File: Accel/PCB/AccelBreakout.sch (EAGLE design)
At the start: 9 parts, among them U1 MMA8653FCR1

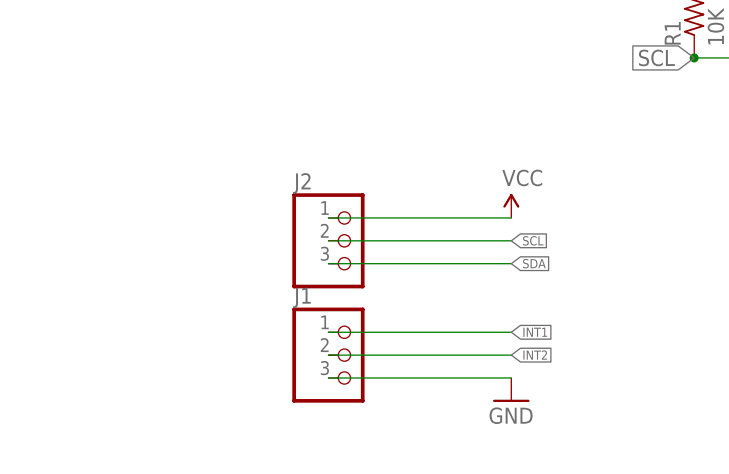
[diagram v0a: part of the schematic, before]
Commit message: added reverse voltage protection
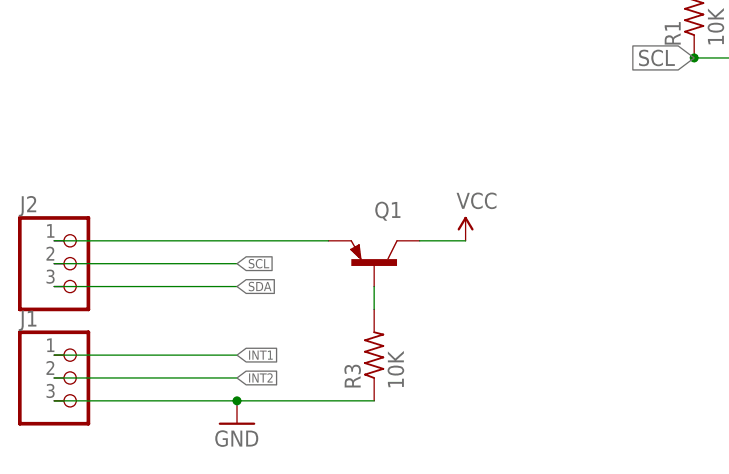
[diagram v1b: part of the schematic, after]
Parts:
- added Q1: MMBTA56-SOT23, transistor-pnp:MMBTA56-SOT23
- added R3: 10K, AccelBreakout:R-US_R0603
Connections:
- new net N$1: J2.1, Q1.E
- new net N$2: Q1.B, R3.2
- net GND: now also R3.1
- net VCC: now also Q1.C; no longer J2.1
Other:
- moved on the sheet: J1, J2
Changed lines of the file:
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@@
 <?xml version="1.0" encoding="utf-8"?>
 <!DOCTYPE eagle SYSTEM "eagle.dtd">
-<eagle version="7.1.0">
+<eagle version="7.6.0">
 <drawing>
 <settings>
@@
 <setting verticaltext="up"/>
 </settings>
-<grid distance="0.1" unitdist="inch" unit="inch" style="lines" multiple="1" display="yes" altdistance="0.01" altunitdist="inch" altunit="inch"/>
+<grid distance="0.1" unitdist="inch" unit="inch" style="lines" multiple="1" display="no" altdistance="0.01" altunitdist="inch" altunit="inch"/>
 <layers>
 <layer number="1" name="Top" color="4" fill="1" visible="no" active="no"/>
 <layer number="2" name="Route2" color="1" fill="3" visible="no" active="no"/>
 <layer number="3" name="Route3" color="4" fill="3" visible="no" active="no"/>
+<layer number="4" name="Route4" color="1" fill="4" visible="no" active="no"/>
+<layer number="5" name="Route5" color="4" fill="4" visible="no" active="no"/>
+<layer number="6" name="Route6" color="1" fill="8" visible="no" active="no"/>
+<layer number="7" name="Route7" color="4" fill="8" visible="no" active="no"/>
+<layer number="8" name="Route8" color="1" fill="2" visible="no" active="no"/>
+<layer number="9" name="Route9" color="4" fill="2" visible="no" active="no"/>
+<layer number="10" name="Route10" color="1" fill="7" visible="no" active="no"/>
+<layer number="11" name="Route11" color="4" fill="7" visible="no" active="no"/>
+<layer number="12" name="Route12" color="1" fill="5" visible="no" active="no"/>
+<layer number="13" name="Route13" color="4" fill="5" visible="no" active="no"/>
 <layer number="14" name="Route14" color="1" fill="6" visible="no" active="no"/>
 <layer number="15" name="Route15" color="4" fill="6" visible="no" active="no"/>
@@
 <part name="J1" library="AccelBreakout" deviceset="PINHD-1X3" device=""/>
 <part name="FRAME1" library="frames" deviceset="LETTER_L" device=""/>
+<part name="Q1" library="transistor-pnp" deviceset="*-?" device="SOT23" technology="MMBTA56"/>
+<part name="R3" library="AccelBreakout" deviceset="R-US_" device="R0603" value="10K"/>
 </parts>
 <sheets>
@@
 <instance part="R1" gate="G$1" x="20.32" y="60.96" rot="R90"/>
 <instance part="R2" gate="G$1" x="83.82" y="66.04" rot="R90"/>
-<instance part="SUPPLY1" gate="G$1" x="0" y="38.1"/>
-<instance part="GND1" gate="1" x="0" y="17.78"/>
-<instance part="J2" gate="A" x="-17.78" y="35.56"/>
-<instance part="J1" gate="A" x="-17.78" y="22.86"/>
+<instance part="SUPPLY1" gate="G$1" x="-5.08" y="35.56"/>
+<instance part="GND1" gate="1" x="-30.48" y="15.24"/>
+<instance part="J2" gate="A" x="-48.26" y="33.02"/>
+<instance part="J1" gate="A" x="-48.26" y="20.32"/>
 <instance part="FRAME1" gate="G$1" x="-86.36" y="-53.34"/>
 <instance part="FRAME1" gate="G$2" x="60.96" y="-53.34"/>
+<instance part="Q1" gate="D" x="-15.24" y="33.02" smashed="yes" rot="R90">
+<attribute name="NAME" x="-15.24" y="38.1" size="1.778" layer="95"/>
+</instance>
+<instance part="R3" gate="G$1" x="-15.24" y="22.86" rot="R90"/>
 </instances>
 <busses>
@@
 </segment>
 <segment>
+<pinref part="Q1" gate="D" pin="C"/>
 <pinref part="SUPPLY1" gate="G$1" pin="VCC"/>
-<wire x1="-20.32" y1="38.1" x2="0" y2="38.1" width="0.1524" layer="91"/>
-<pinref part="J2" gate="A" pin="1"/>
+<wire x1="-10.16" y1="35.56" x2="-5.08" y2="35.56" width="0.1524" layer="91"/>
 </segment>
 </net>
@@
 <segment>
 <pinref part="GND1" gate="1" pin="GND"/>
-<wire x1="0" y1="20.32" x2="-20.32" y2="20.32" width="0.1524" layer="91"/>
+<wire x1="-30.48" y1="17.78" x2="-50.8" y2="17.78" width="0.1524" layer="91"/>
 <pinref part="J1" gate="A" pin="3"/>
+<pinref part="R3" gate="G$1" pin="1"/>
+<wire x1="-30.48" y1="17.78" x2="-15.24" y2="17.78" width="0.1524" layer="91"/>
+<junction x="-30.48" y="17.78"/>
 </segment>
 </net>
@@
 <segment>
 <pinref part="J2" gate="A" pin="3"/>
-<wire x1="-20.32" y1="33.02" x2="0" y2="33.02" width="0.1524" layer="91"/>
-<label x="0" y="33.02" size="1.016" layer="95" xref="yes"/>
+<wire x1="-50.8" y1="30.48" x2="-30.48" y2="30.48" width="0.1524" layer="91"/>
+<label x="-30.48" y="30.48" size="1.016" layer="95" xref="yes"/>
 </segment>
 </net>
@@
 <segment>
 <pinref part="J2" gate="A" pin="2"/>
-<wire x1="-20.32" y1="35.56" x2="0" y2="35.56" width="0.1524" layer="91"/>
-<label x="0" y="35.56" size="1.016" layer="95" xref="yes"/>
+<wire x1="-50.8" y1="33.02" x2="-30.48" y2="33.02" width="0.1524" layer="91"/>
+<label x="-30.48" y="33.02" size="1.016" layer="95" xref="yes"/>
 </segment>
 </net>
@@
 </segment>
 <segment>
-<label x="0" y="25.4" size="1.016" layer="95" xref="yes"/>
-<wire x1="-20.32" y1="25.4" x2="0" y2="25.4" width="0.1524" layer="91"/>
+<label x="-30.48" y="22.86" size="1.016" layer="95" xref="yes"/>
+<wire x1="-50.8" y1="22.86" x2="-30.48" y2="22.86" width="0.1524" layer="91"/>
 <pinref part="J1" gate="A" pin="1"/>
 </segment>
@@
 </segment>
 <segment>
-<label x="0" y="22.86" size="1.016" layer="95" xref="yes"/>
-<wire x1="-20.32" y1="22.86" x2="0" y2="22.86" width="0.1524" layer="91"/>
+<label x="-30.48" y="20.32" size="1.016" layer="95" xref="yes"/>
+<wire x1="-50.8" y1="20.32" x2="-30.48" y2="20.32" width="0.1524" layer="91"/>
 <pinref part="J1" gate="A" pin="2"/>
 </segment>
 </net>
+<net name="N$2" class="0">
+<segment>
+<pinref part="R3" gate="G$1" pin="2"/>
+<pinref part="Q1" gate="D" pin="B"/>
+<wire x1="-15.24" y1="27.94" x2="-15.24" y2="30.48" width="0.1524" layer="91"/>
+</segment>
+</net>
+<net name="N$1" class="0">
+<segment>
+<pinref part="Q1" gate="D" pin="E"/>
+<pinref part="J2" gate="A" pin="1"/>
+<wire x1="-20.32" y1="35.56" x2="-50.8" y2="35.56" width="0.1524" layer="91"/>
+</segment>
+</net>
